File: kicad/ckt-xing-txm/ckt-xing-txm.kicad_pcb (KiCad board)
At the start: 2 copper layers, 76.2 x 63.5 mm, 49 parts, among them J1 Screw_Terminal_01x02, J2 SM04B-SRSS, J3 Conn_02x05_Counter_Clockwise, J4 SM04B-SRSS, J5 SM04B-SRSS, J6 Screw_Terminal_01x02, J7 Screw_Terminal_01x02, Q1 ZXMS6004FF, Q2 ZXMS6004FF, SW1 SW_DIP_x05, U1 PAM8301, U2 ATtiny861A-S, U3 AP7381-33Y, U4 W25Q128JVS

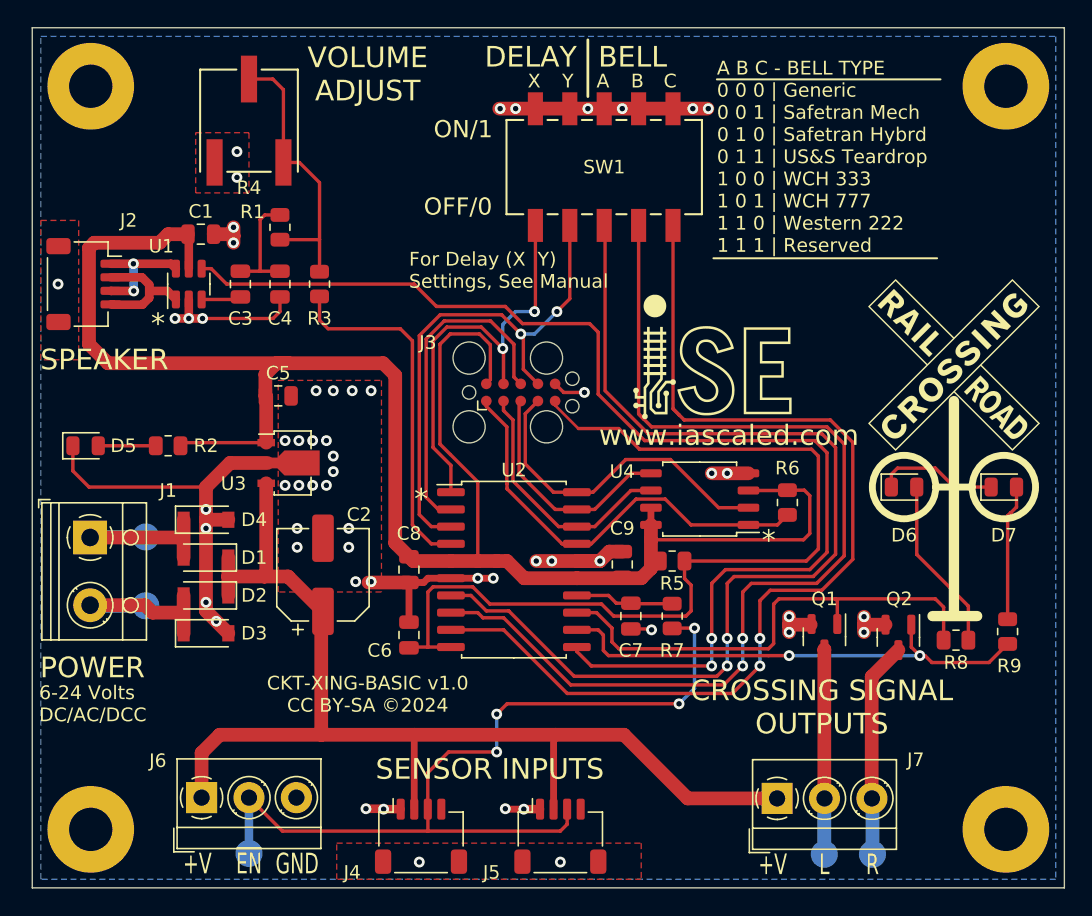
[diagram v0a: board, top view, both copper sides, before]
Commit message: Initial layout of TXM board
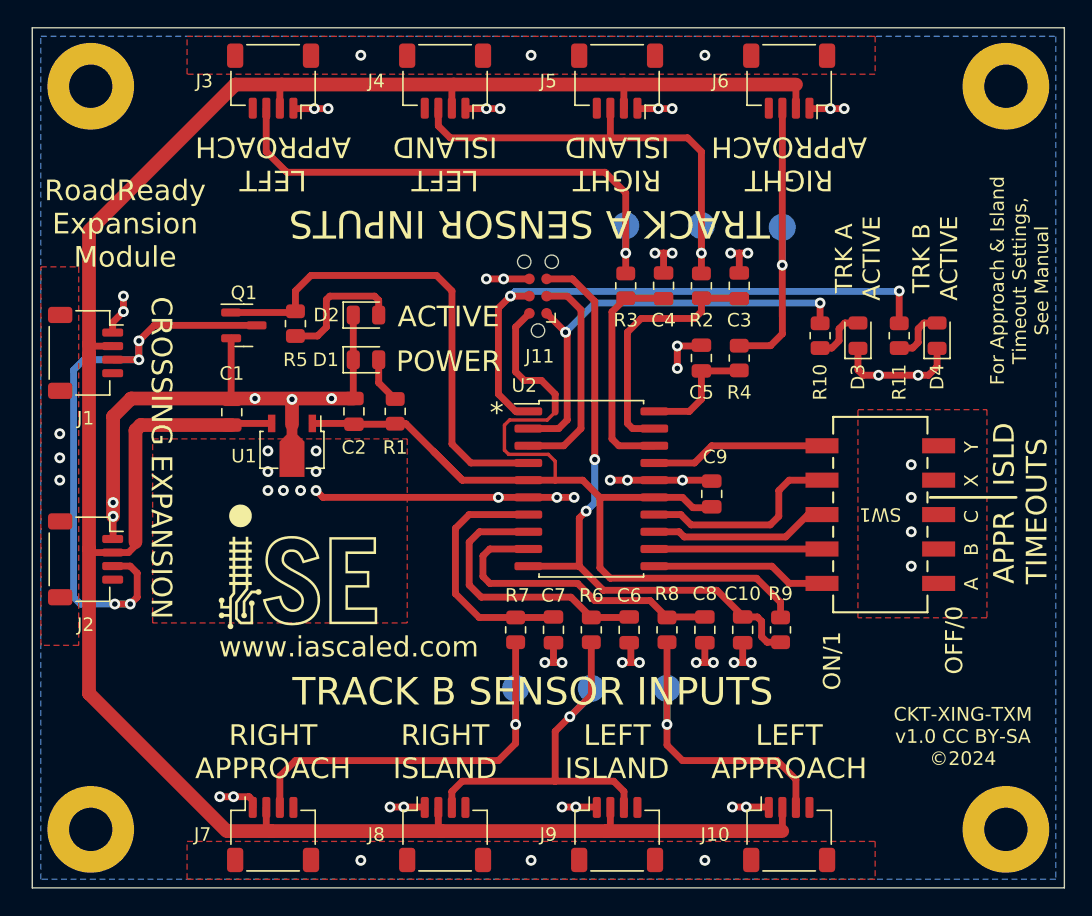
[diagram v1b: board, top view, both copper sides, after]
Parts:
- removed D5: GREEN LED, LED_SMD:LED_0805_2012Metric
- removed D6, D7: RED LED, LED_SMD:LED_0805_2012Metric
- removed G***: LOGO, ISE_Generic:IMG_RRXING
- removed Q2: ZXMS6004FF, Package_TO_SOT_SMD:SOT-23
- removed U3: AP7381-33Y, ISE_Generic:SOT-89-3
- removed U4: W25Q128JVS, Package_SO:SOIC-8_5.23x5.23mm_P1.27mm
- added C10: 1uF, Capacitor_SMD:C_0805_2012Metric, F.Cu at (77.9, 63.5)
- added J10: SM04B-SRSS, Connector_JST:JST_SH_SM04B-SRSS-TB_1x04-1MP_P1.00mm_Horizontal, F.Cu at (81.3, 78.6)
- added J11: Conn_AVR_TagConnect_TC2030, Connector:Tag-Connect_TC2030-IDC-NL_2x03_P1.27mm_Vertical, F.Cu at (62.7, 38.9)
- added J8: SM04B-SRSS, Connector_JST:JST_SH_SM04B-SRSS-TB_1x04-1MP_P1.00mm_Horizontal, F.Cu at (55.9, 78.6)
- added J9: SM04B-SRSS, Connector_JST:JST_SH_SM04B-SRSS-TB_1x04-1MP_P1.00mm_Horizontal, F.Cu at (68.6, 78.6)
- added R10: 1k, Resistor_SMD:R_0805_2012Metric, F.Cu at (83.6, 41.8)
- added R11: 1k, Resistor_SMD:R_0805_2012Metric, F.Cu at (89.4, 41.8)
- added TP6: TestPoint, TestPoint:TestPoint_Pad_D2.0mm, B.Cu at (72.3, 67.8)
- C2: value 68uF -> 22uF; footprint Capacitor_SMD:CP_Elec_6.3x5.8 -> Capacitor_SMD:C_0805_2012Metric
- C3, C8: value 0.1uF -> 1uF
- C4: value 470pF -> 1uF
- C5: value 22uF -> 1uF
- D1: value CDBM140G -> GREEN LED; footprint Diode_SMD:D_SOD-123 -> LED_SMD:LED_0805_2012Metric
- D2: value CDBM140G -> RED; footprint Diode_SMD:D_SOD-123 -> LED_SMD:LED_0805_2012Metric
- D3, D4: value CDBM140G -> AMBER; footprint Diode_SMD:D_SOD-123 -> LED_SMD:LED_0805_2012Metric
- J1: value Screw_Terminal_01x02 -> SM04B-SRSS; footprint TerminalBlock_RND:TerminalBlock_RND_205-00012_1x02_P5.00mm_Horizontal -> Connector_JST:JST_SH_SM04B-SRSS-TB_1x04-1MP_P1.00mm_Horizontal
- J3: value Conn_02x05_Counter_Clockwise -> SM04B-SRSS; footprint Connector:Tag-Connect_TC2050-IDC-FP_2x05_P1.27mm_Vertical -> Connector_JST:JST_SH_SM04B-SRSS-TB_1x04-1MP_P1.00mm_Horizontal
- J6, J7: value Screw_Terminal_01x02 -> SM04B-SRSS; footprint TerminalBlock_MetzConnect:TerminalBlock_MetzConnect_Type059_RT06303HBWC_1x03_P3.50mm_Horizontal -> Connector_JST:JST_SH_SM04B-SRSS-TB_1x04-1MP_P1.00mm_Horizontal
- R1: value 100k -> 1k
- R3, R5, R6: value 10k -> 1k
- R4: value 10k -> 1k; footprint ISE_UltraLibrarian:POT_3361P_BRN -> Resistor_SMD:R_0805_2012Metric
- R9: value 1k -> 10k
- U1: value PAM8301 -> AP7381-33Y; footprint Package_TO_SOT_SMD:SOT-23-6 -> ISE_Generic:SOT-89-3
- moved J6 68.4 mm to (81.3, 23.0), turned to 180 degrees
- moved TP3 60.7 mm to (80.8, 33.8)
- moved J5 55.9 mm to (68.6, 23.0), turned to 180 degrees
- moved J4 55.8 mm to (55.9, 23.0), turned to 180 degrees
- moved D4 55.7 mm to (92.2, 41.8), turned to 90 degrees
- moved D3 52.9 mm to (86.4, 41.8), turned to 90 degrees
- moved Q1 48.6 mm to (41.0, 41.0), turned to 0 degrees
- moved TP1 47.0 mm to (74.8, 33.7)
- moved TP2 45.2 mm to (69.2, 33.7)
- moved R2 41.1 mm to (74.8, 38.1), turned to -90 degrees
- moved R4 40.2 mm to (77.6, 43.4), turned to -90 degrees
- moved J7 37.3 mm to (43.2, 78.6)
- moved C3 36.8 mm to (77.6, 38.1)
- moved R5 32.9 mm to (44.8, 40.9), turned to 90 degrees
- moved SW1 32.8 mm to (88.0, 55.0), turned to 180 degrees
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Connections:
- C1 pad 1: +3.3V -> /VIN
- C2 pad 1: /VIN -> +3.3V
- C3 pad 1: Net-(C3-Pad1) -> /~{ISLAND_1}
- C3 pad 2: Net-(C3-Pad2) -> GND
- C4 pad 1: Net-(C3-Pad2) -> /~{APPR_A_1}
- C5 pad 1: +3.3V -> /~{APPR_B_1}
- C6 pad 1: /~{RESET} -> /~{ISLAND_2}
- C7 pad 1: /EN1x -> /~{APPR_A_2}
- C8 pad 1: +3.3V -> /~{APPR_B_2}
- D1 pad 1: /VIN -> GND
- D2 pad 1: /VIN -> GND
- D3 pad 1: Net-(D2-Pad2) -> GND
- D3 pad 2: GND -> Net-(D3-Pad2)
- D4 pad 1: Net-(D1-Pad2) -> GND
- D4 pad 2: GND -> Net-(D4-Pad2)
- J1 pad 1: Net-(D1-Pad2) -> GND
- J1 pad 2: Net-(D2-Pad2) -> /VIN
- J2 pad 1: Net-(J2-Pad1) -> GND
- J2 pad 2: Net-(J2-Pad2) -> /VIN
- J2 pad 3: Net-(J2-Pad1) -> Net-(J1-Pad3)
- J2 pad 4: Net-(J2-Pad2) -> unconnected-(J2-Pad4)
- J3 pad 1: /~{FLASH_CS} -> GND
- J3 pad 2: /FLASH_SCK -> /VIN
- J3 pad 3: /FLASH_MOSI -> Net-(J3-Pad3)
- J3 pad 4: /FLASH_MISO -> unconnected-(J3-Pad4)
- J4 pad 3: /EN1 -> Net-(R2-Pad1)
- J5 pad 3: /EN1 -> Net-(R2-Pad1)
- J6 pad 1: /VIN -> GND
- J6 pad 2: /EN1 -> /VIN
- J6 pad 3: GND -> Net-(J6-Pad3)
- J7 pad 1: /VIN -> GND
- J7 pad 2: Net-(Q1-Pad3) -> /VIN
- J7 pad 3: Net-(Q2-Pad3) -> Net-(J7-Pad3)
- Q1 pad 1: /OUT_L -> /~{ENABLE}
- Q1 pad 3: Net-(Q1-Pad3) -> Net-(J1-Pad3)
- R1 pad 1: Net-(C3-Pad2) -> Net-(D1-Pad2)
- R1 pad 2: Net-(R1-Pad2) -> +3.3V
- R2 pad 1: Net-(D5-Pad2) -> Net-(R2-Pad1)
- R2 pad 2: +3.3V -> /~{ISLAND_1}
- R3 pad 1: Net-(R1-Pad2) -> Net-(J3-Pad3)
- R3 pad 2: /PWM -> /~{APPR_A_1}
- R4 pad 1: GND -> Net-(J6-Pad3)
- R4 pad 2: Net-(R1-Pad2) -> /~{APPR_B_1}
- R5 pad 1: /~{RESET} -> Net-(D2-Pad2)
- R5 pad 2: +3.3V -> /~{ENABLE}
- R6 pad 1: +3.3V -> Net-(J8-Pad3)
- R6 pad 2: /~{FLASH_CS} -> /~{ISLAND_2}
- R7 pad 1: /EN1 -> Net-(J7-Pad3)
- R7 pad 2: /EN1x -> /~{APPR_A_2}
- R8 pad 2: /OUT_L -> /~{APPR_B_2}
- R9 pad 1: Net-(D7-Pad2) -> /~{RESET}
- R9 pad 2: /OUT_R -> +3.3V
- SW1 pad 1: /AVR_MOSI -> GND
- SW1 pad 10: GND -> /SW5
- SW1 pad 2: /AVR_SCK -> GND
- SW1 pad 3: /SW3 -> GND
- SW1 pad 4: /SW4 -> GND
- SW1 pad 5: /SW5 -> GND
- SW1 pad 6: GND -> /SW1
- SW1 pad 7: GND -> /SW2
- SW1 pad 8: GND -> /SW3
- SW1 pad 9: GND -> /SW4
- TP1 pad 1: Net-(D1-Pad2) -> Net-(R2-Pad1)
- TP2 pad 1: Net-(D2-Pad2) -> Net-(J3-Pad3)
- TP3 pad 1: /EN1 -> Net-(J6-Pad3)
- TP4 pad 1: Net-(Q1-Pad3) -> Net-(J8-Pad3)
- TP5 pad 1: Net-(Q2-Pad3) -> Net-(J7-Pad3)
- U1 pad 1: Net-(J2-Pad2) -> +3.3V
- U1 pad 3: Net-(C3-Pad1) -> /VIN
- U2 pad 11: /~{SD} -> /SW5
- U2 pad 12: /OUT_R -> /SW4
- U2 pad 13: /OUT_L -> /SW3
- U2 pad 14: /EN1x -> /SW2
- U2 pad 17: /~{FLASH_CS} -> /SW1
- U2 pad 18: /FLASH_SCK -> /~{APPR_A_1}
- U2 pad 19: /FLASH_MOSI -> /~{ISLAND_1}
- U2 pad 20: /FLASH_MISO -> /~{APPR_B_1}
- U2 pad 4: /PWM -> /~{ENABLE}
- U2 pad 7: /SW3 -> /~{APPR_A_2}
- U2 pad 8: /SW4 -> /~{ISLAND_2}
- U2 pad 9: /SW5 -> /~{APPR_B_2}
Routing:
- net /VIN: track 84.9 -> 184.8 mm
- net /~{SD}: track 88.1 -> 0.00 mm, vias 2 -> 0
- net /SW4: track 77.1 -> 12.4 mm, vias 2 -> 0
- net /SW3: track 77.0 -> 13.2 mm, vias 2 -> 0
- net /EN1: track 63.7 -> 0.00 mm, vias 4 -> 0
- net /SW5: track 75.6 -> 12.9 mm, vias 2 -> 0
- net +3.3V: track 136.0 -> 77.0 mm
- net Net-(J1-Pad3): track 0.00 -> 45.9 mm, vias 0 -> 4
- net Net-(J3-Pad3): track 0.00 -> 39.0 mm, vias 0 -> 1
- net /OUT_L: track 36.6 -> 0.00 mm
- net /OUT_R: track 36.6 -> 0.00 mm, vias 2 -> 0
- net /~{ENABLE}: track 0.00 -> 36.3 mm
- net Net-(R2-Pad1): track 0.00 -> 34.7 mm, vias 0 -> 1
- net /~{FLASH_CS}: track 32.0 -> 0.00 mm
- net Net-(J7-Pad3): track 0.00 -> 30.9 mm, vias 0 -> 1
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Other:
- board text added: "ACTIVE"
- board text added: "APPR"
- board text added: "CKT-XING-TXM v1.0 CC BY-SA ©2024"
- board text added: "CROSSING EXPANSION"
- board text added: "For Approach & Island Timeout Settings, See Manual"
- board text added: "ISLD"
- board text added: "LEFT APPROACH"
- board text added: "LEFT ISLAND"
- board text added: "ON/1"
- board text added: "RIGHT APPROACH"
- board text added: "RIGHT ISLAND"
- board text added: "RoadReady Expansion Module"
- board text added: "TIMEOUTS"
- board text added: "TRACK A SENSOR INPUTS"
- board text added: "TRACK B SENSOR INPUTS"
- board text added: "TRK A ACTIVE"
- board text added: "TRK B ACTIVE"
- board text removed: "+V"
- board text removed: "6-24 Volts DC/AC/DCC"
- board text removed: "A B C - BELL TYPE 0 0 0 | Generic 0 0 1 | Safetran Mech 0 1 0 | Safetran Hybrd 0 1 1 | US&S Teardrop 1 0 0 | WCH 333 1 0 1 | WCH 777 1 1 0 | Western 222 1 1 1 | Reserved"
- board text removed: "BELL"
- board text removed: "CKT-XING-BASIC v1.0 CC BY-SA ©2024"
- board text removed: "CROSSING SIGNAL OUTPUTS"
- board text removed: "DELAY"
- board text removed: "For Delay (X Y) Settings, See Manual"
- board text removed: "GND"
- board text removed: "L"
- board text removed: "R"
- board text removed: "SENSOR INPUTS"
- board text removed: "SPEAKER"
- board text removed: "VOLUME ADJUST"
- board text removed: "~{EN}"

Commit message: Review updates
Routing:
- net Net-(J8-Pad3): track 29.8 -> 31.3 mm
- net Net-(J10-Pad3): track 22.9 -> 21.8 mm
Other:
- board text added: "APPROACH"
- board text added: "CKT-XING-TXM v1.0 CC BY-SA"
- board text added: "ISLAND"
- board text added: "©2024"
- board text removed: "APPR"
- board text removed: "CKT-XING-TXM v1.0 CC BY-SA ©2024"
- board text removed: "ISLD"
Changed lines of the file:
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@@
       (effects (font (size 1 1) (thickness 0.15)))
     )
-    (fp_text user "OFF/0" (at -5.461 -9.271 90 unlocked) (layer "F.SilkS")
+    (fp_text user "OFF/0" (at -3.556 -11.303 90 unlocked) (layer "F.SilkS")
       (effects (font (size 1.27 1.27) (thickness 0.15)))
     )
@@
     ) (layer "F.SilkS") (width 0) (fill solid))
   (gr_rect locked (start 25.4 19.05) (end 101.6 82.55) (layer "Edge.Cuts") (width 0.1) (fill none))
-  (gr_text "RIGHT\nAPPROACH\n" (at 43.18 72.517) (layer "F.SilkS")
+  (gr_text "LEFT\nAPPROACH\n" (at 43.18 72.517) (layer "F.SilkS")
     (effects (font (size 1.524 1.524) (thickness 0.3048)))
   )
@@
     (effects (font (size 1.524 1.524) (thickness 0.3048)))
   )
-  (gr_text "APPR" (at 97.155 57.404 90) (layer "F.SilkS")
-    (effects (font (size 1.524 1.524) (thickness 0.3048)))
+  (gr_text "APPROACH" (at 97.155 58.293 90) (layer "F.SilkS")
+    (effects (font (size 1.524 1.016) (thickness 0.254)))
   )
   (gr_text "B" (at 94.742 58.039 90) (layer "F.SilkS")
@@
     (effects (font (size 1.016 1.016) (thickness 0.1524)) (justify left))
   )
-  (gr_text "CKT-XING-TXM\nv1.0 CC BY-SA \n©2024" (at 94.107 71.374) (layer "F.SilkS")
+  (gr_text "CKT-XING-TXM\nv1.0 CC BY-SA" (at 94.234 72.644) (layer "F.SilkS")
     (effects (font (size 1.016 1.016) (thickness 0.1524)))
   )
-  (gr_text "LEFT\nAPPROACH\n" (at 81.28 72.517) (layer "F.SilkS")
+  (gr_text "©2024" (at 90.932 75.438) (layer "F.SilkS")
+    (effects (font (size 1 1) (thickness 0.15)))
+  )
+  (gr_text "RIGHT\nAPPROACH\n" (at 81.28 72.517) (layer "F.SilkS")
     (effects (font (size 1.524 1.524) (thickness 0.3048)))
   )
@@
     (effects (font (size 1.524 1.524) (thickness 0.3048)))
   )
-  (gr_text "RIGHT\nISLAND" (at 55.88 72.517) (layer "F.SilkS")
+  (gr_text "LEFT\nISLAND" (at 55.88 72.517) (layer "F.SilkS")
     (effects (font (size 1.524 1.524) (thickness 0.3048)))
   )
@@
     (effects (font (size 1.524 1.524) (thickness 0.3048)))
   )
-  (gr_text "LEFT\nISLAND" (at 68.58 72.517) (layer "F.SilkS")
+  (gr_text "RIGHT\nISLAND" (at 68.58 72.517) (layer "F.SilkS")
     (effects (font (size 1.524 1.524) (thickness 0.3048)))
   )
@@
     (effects (font (size 1.524 1.524) (thickness 0.3048)))
   )
-  (gr_text "ISLD" (at 97.155 50.546 90) (layer "F.SilkS")
-    (effects (font (size 1.524 1.524) (thickness 0.3048)))
+  (gr_text "ISLAND" (at 97.155 50.546 90) (layer "F.SilkS")
+    (effects (font (size 1.524 1.016) (thickness 0.254)))
   )
   (gr_text "LEFT\nISLAND" (at 55.88 29.083 180) (layer "F.SilkS")
@@
   (via (at 61.087 70.485) (size 0.8) (drill 0.4) (layers "F.Cu" "B.Cu") (net 32))
   (segment (start 61.087 67.818) (end 61.087 70.485) (width 0.508) (layer "B.Cu") (net 32))
+  (segment (start 72.263 69.215) (end 76.2 73.152) (width 0.508) (layer "F.Cu") (net 36))
+  (segment (start 72.263 64.4125) (end 72.263 69.215) (width 0.508) (layer "F.Cu") (net 36))
   (segment (start 81.78 74.541) (end 81.78 76.613) (width 0.508) (layer "F.Cu") (net 36))
-  (segment (start 72.263 72.009) (end 73.406 73.152) (width 0.508) (layer "F.Cu") (net 36))
-  (segment (start 72.263 64.4125) (end 72.263 72.009) (width 0.508) (layer "F.Cu") (net 36))
-  (segment (start 73.406 73.152) (end 80.391 73.152) (width 0.508) (layer "F.Cu") (net 36))
   (segment (start 80.391 73.152) (end 81.78 74.541) (width 0.508) (layer "F.Cu") (net 36))
-  (via (at 72.263 70.485) (size 0.8) (drill 0.4) (layers "F.Cu" "B.Cu") (net 36))
-  (segment (start 72.263 67.818) (end 72.263 70.485) (width 0.508) (layer "B.Cu") (net 36))
+  (segment (start 76.2 73.152) (end 80.391 73.152) (width 0.508) (layer "F.Cu") (net 36))
+  (via (at 73.533 70.485) (size 0.8) (drill 0.4) (layers "F.Cu" "B.Cu") (net 36))
+  (segment (start 72.263 69.215) (end 73.533 70.485) (width 0.508) (layer "B.Cu") (net 36))
+  (segment (start 72.263 67.818) (end 72.263 69.215) (width 0.508) (layer "B.Cu") (net 36))
   (segment (start 44.831 38.481) (end 45.974 37.338) (width 0.508) (layer "F.Cu") (net 38))
   (segment (start 57.785 51.181) (end 62.025 51.181) (width 0.508) (layer "F.Cu") (net 38))
@@
   (segment (start 57.15 74.676) (end 64.008 74.676) (width 0.508) (layer "F.Cu") (net 42))
   (segment (start 69.088 76.605) (end 69.08 76.613) (width 0.508) (layer "F.Cu") (net 42))
-  (via (at 65.0875 69.9135) (size 0.8) (drill 0.4) (layers "F.Cu" "B.Cu") (net 42))
-  (segment (start 66.675 67.818) (end 66.675 68.326) (width 0.508) (layer "B.Cu") (net 42))
-  (segment (start 66.675 68.326) (end 65.0875 69.9135) (width 0.508) (layer "B.Cu") (net 42))
+  (via (at 64.008 70.993) (size 0.8) (drill 0.4) (layers "F.Cu" "B.Cu") (net 42))
+  (segment (start 64.008 70.993) (end 66.675 68.326) (width 0.508) (layer "B.Cu") (net 42))
+  (segment (start 66.675 68.326) (end 66.675 67.818) (width 0.508) (layer "B.Cu") (net 42))
   (segment (start 84.4315 42.6955) (end 84.963 42.164) (width 0.508) (layer "F.Cu") (net 43))
   (segment (start 84.963 42.164) (end 84.963 41.275) (width 0.508) (layer "F.Cu") (net 43))
